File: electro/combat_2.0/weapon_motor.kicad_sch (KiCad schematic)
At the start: 12 parts

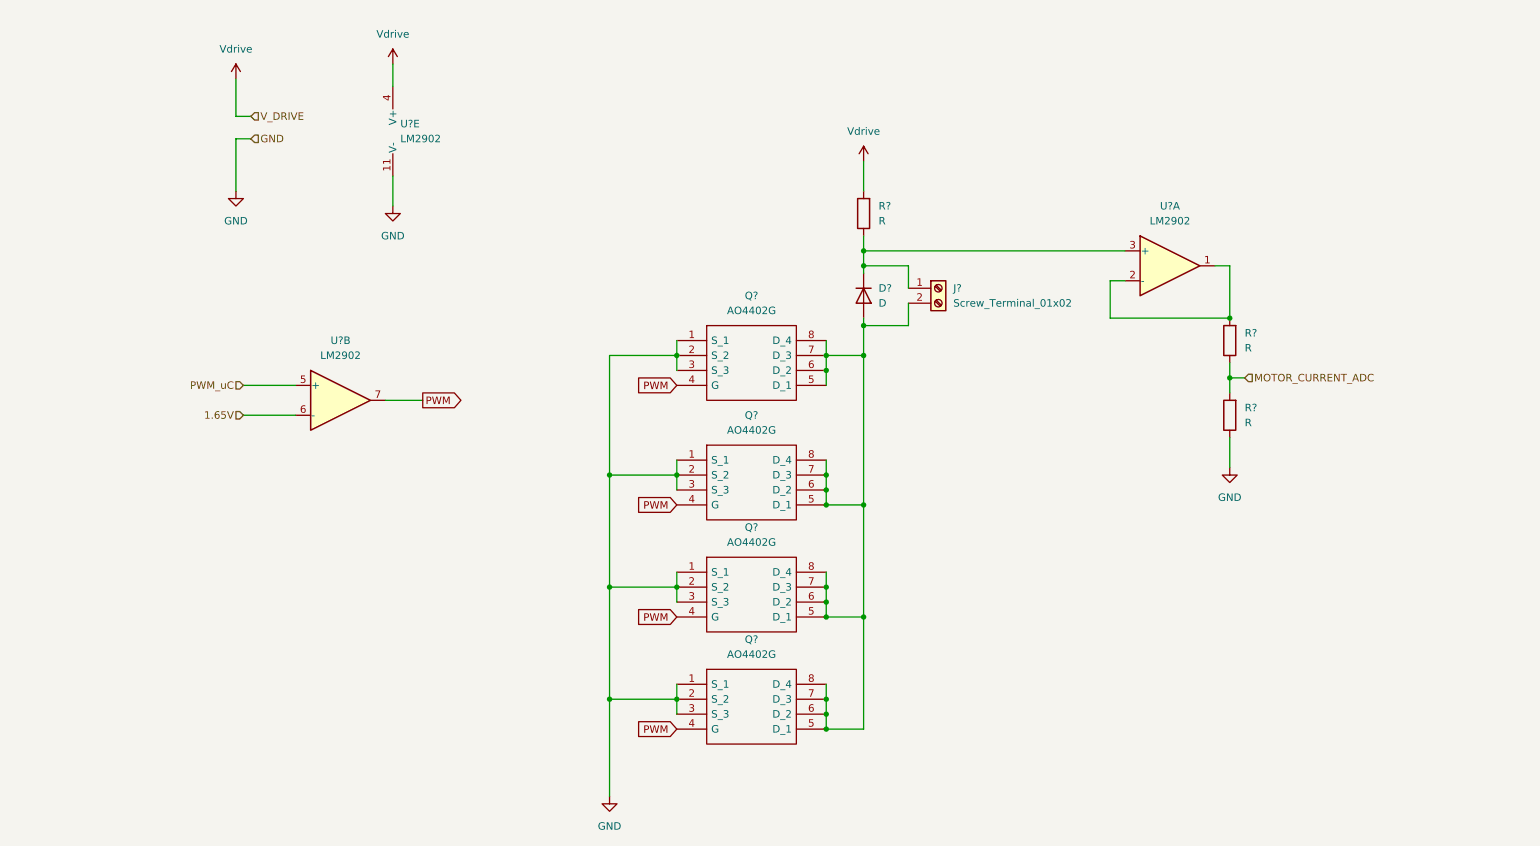
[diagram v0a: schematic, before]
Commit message: 20A Current sensor
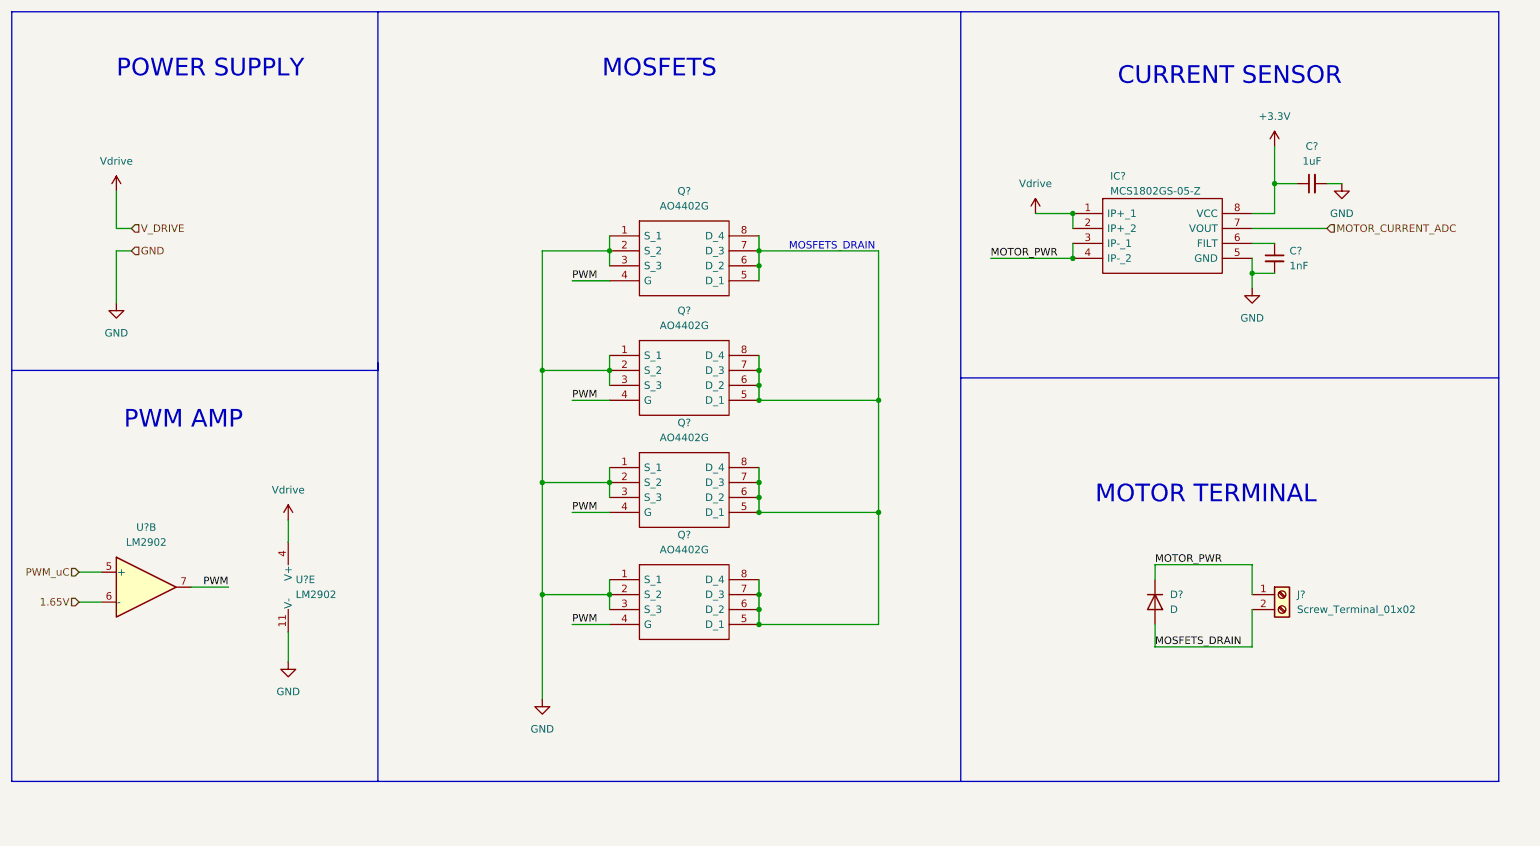
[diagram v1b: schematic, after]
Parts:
- removed R? (x3): R, symbol Device:R
- removed U?: LM2902, symbol Amplifier_Operational:LM2902
- added C?: 1uF, Capacitor_SMD:C_1206_3216Metric, symbol Device:C_Small
- added C?: 1nF, Capacitor_SMD:C_1206_3216Metric, symbol Device:C_Small
- added IC?: MCS1802GS-05-Z, MCS1802GS:SOIC127P600X175-8N, symbol MCS1802GS-05-Z:MCS1802GS-05-Z
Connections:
- net GND: now also C?.2, C?.2, IC?.5 (GND)
- net MOTOR_CURRENT_ADC: now also IC?.7 (VOUT)
- net Vdrive: now also IC?.1 (IP+_1), IC?.2 (IP+_2)
- net MOTOR_PWR: now reaches D?.1 (K), J?.1 (Pin_1)
- net MOTOR_PWR: now also IC?.3 (IP-_1), IC?.4 (IP-_2)
- net at Q?.5 (D_1), Q?.5 (D_1), Q?.5 (D_1)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: no longer D?.2 (A), J?.2 (Pin_2)
- new net: C?.1, IC?.6 (FILT)
- new net +3.3V: C?.1, IC?.8 (VCC)
- new net MOSFETS_DRAIN: D?.2 (A), J?.2 (Pin_2)
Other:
- note added: "CURRENT SENSOR"
- note added: "MOSFETS"
- note added: "MOSFETS_DRAIN"
- note added: "MOTOR TERMINAL"
- note added: "POWER SUPPLY"
- note added: "PWM AMP"
- moved on the sheet: D?, J?, Q?, U?B, U?E

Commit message: PCB V0
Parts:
- added F2: 12A, Capacitor_THT:C_Rect_L13.0mm_W3.0mm_P10.00mm_FKS3_FKP3_MKS4, symbol Device:Polyfuse_Small
- added R3: R, Resistor_SMD:R_0805_2012Metric, symbol Device:R
- C10, C9: renamed from C?; footprint Capacitor_SMD:C_1206_3216Metric -> Capacitor_SMD:C_0805_2012Metric
- D1: renamed from D?; footprint (none) -> Diode_SMD:D_SOD-123F
- J4: renamed from J?; footprint (none) -> TerminalBlock:TerminalBlock_Altech_AK300-2_P5.00mm
- Q1, Q2, Q3, Q4: renamed from Q?; footprint SOIC127P600X175-8N -> MCS1802GS:SOIC127P600X175-8N
- gave numbers to parts that had none: 2
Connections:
- net MOSFETS_DRAIN: now also J4.1 (Pin_1), Q1.5 (D_1), Q1.6 (D_2), Q1.7 (D_3), Q1.8 (D_4), Q2.5 (D_1), Q2.6 (D_2), Q2.7 (D_3), Q2.8 (D_4), Q3.5 (D_1), Q3.6 (D_2), Q3.7 (D_3), Q3.8 (D_4), Q4.5 (D_1), Q4.6 (D_2), Q4.7 (D_3), Q4.8 (D_4); no longer J4.2 (Pin_2)
- net MOTOR_PWR: now also J4.2 (Pin_2), F2.1; no longer IC1.3 (IP-_1), IC1.4 (IP-_2), J4.1 (Pin_1)
- net PWM: now also R3.2; no longer U4.7
- net PWM_uC: now also U4.7, R3.1
- new net: F2.2, IC1.3 (IP-_1), IC1.4 (IP-_2)
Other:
- note added: "Is just 3V3 enough?"
- note removed: "MOSFETS_DRAIN"
- moved on the sheet: J4, U4E

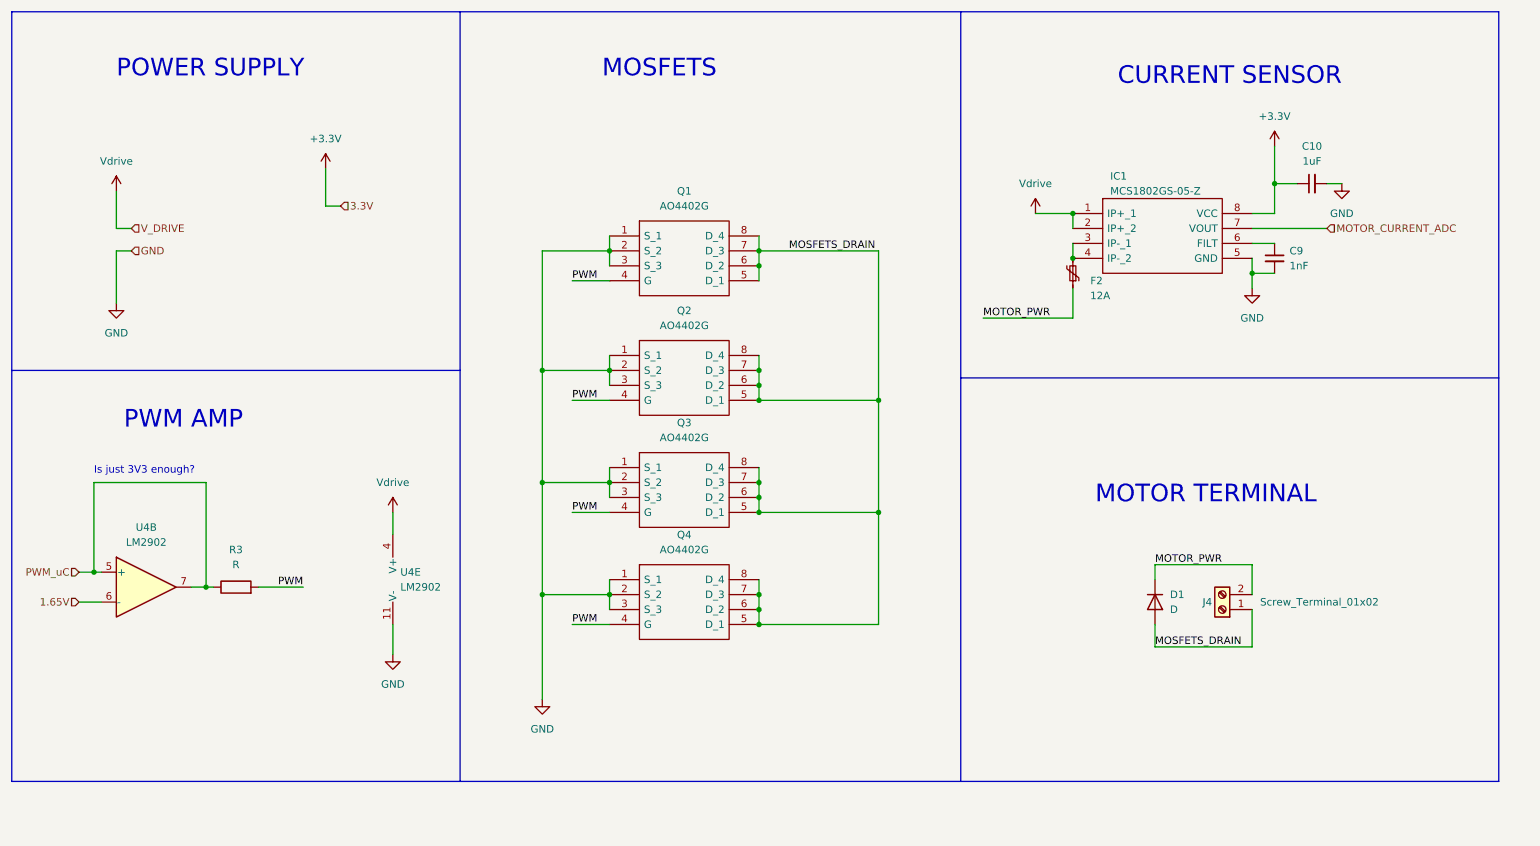
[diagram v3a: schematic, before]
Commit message: Standarized schematic labels
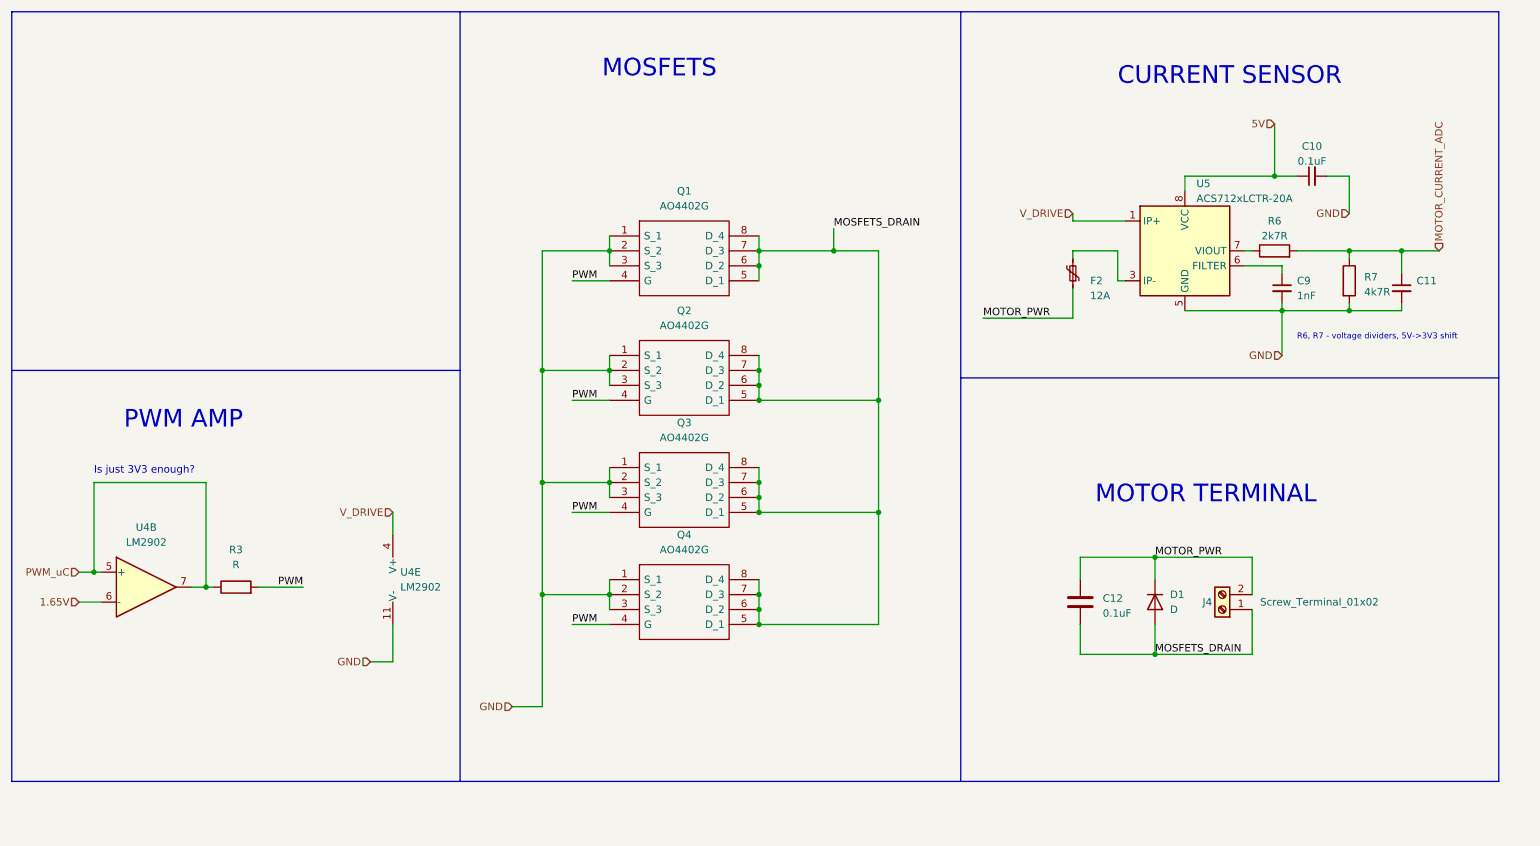
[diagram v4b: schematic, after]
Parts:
- removed IC1: MCS1802GS-05-Z, MCS1802GS:SOIC127P600X175-8N, symbol MCS1802GS-05-Z:MCS1802GS-05-Z
- added C11: ~, Capacitor_SMD:C_0805_2012Metric, symbol Device:C_Small
- added C12: 0.1uF, symbol Device:C
- added R6: 2k7R, symbol Device:R
- added R7: 4k7R, symbol Device:R
- added U5: ACS712xLCTR-20A, Package_SO:SOIC-8_3.9x4.9mm_P1.27mm, symbol Sensor_Current:ACS712xLCTR-20A
- C10: value 1uF -> 0.1uF
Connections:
- net GND: now also C11.2, R7.2, U5.5 (GND)
- net MOSFETS_DRAIN: now also C12.2
- net MOTOR_CURRENT_ADC: now also C11.1, R6.2, R7.1
- net MOTOR_PWR: now also C12.1
- net at F2.2: now also U5.3 (IP-), U5.4 (IP-)
- net at C9.1: now also U5.6 (FILTER)
- net +3.3V renamed 5V
- net 5V: now also U5.8 (VCC)
- net Vdrive renamed V_DRIVE
- net V_DRIVE: now also U5.1 (IP+), U5.2 (IP+)
- new net: R6.1, U5.7 (VIOUT)
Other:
- note added: "R6, R7 - voltage dividers, 5V->3V3 shift"
- note removed: "POWER SUPPLY"
- moved on the sheet: C10, C9

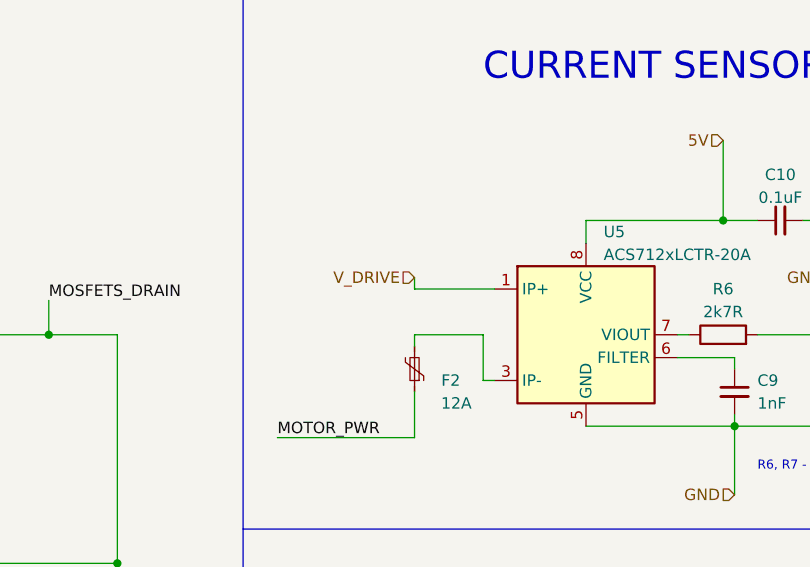
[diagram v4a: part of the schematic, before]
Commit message: Changed resistors to SMD1206 type, hand-soldered version (slightly bigger pads)
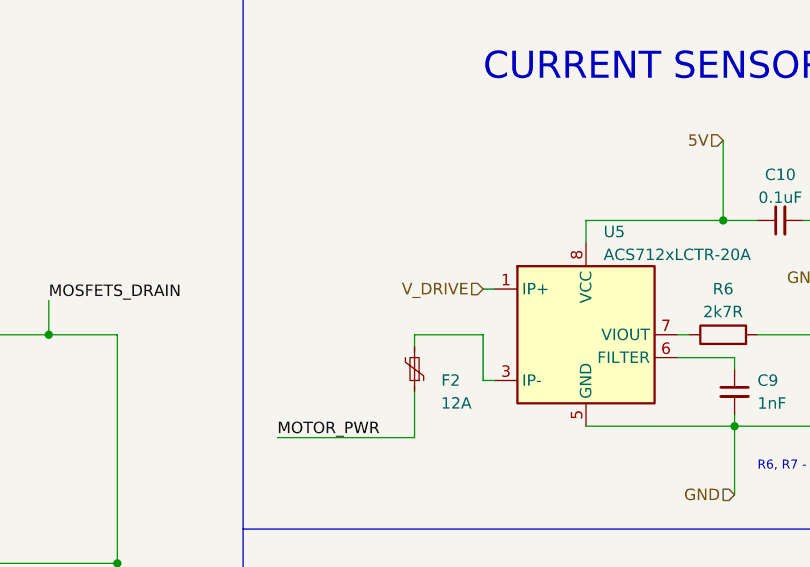
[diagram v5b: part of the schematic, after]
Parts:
- R3: footprint Resistor_SMD:R_0805_2012Metric -> Resistor_SMD:R_1206_3216Metric_Pad1.30x1.75mm_HandSolder
- R6, R7: footprint (none) -> Resistor_SMD:R_1206_3216Metric_Pad1.30x1.75mm_HandSolder
- U4: footprint (none) -> Package_SO:SOIC-14_3.9x8.7mm_P1.27mm
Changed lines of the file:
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@@
     (stroke (width 0) (type default))
   )
-  (wire (pts (xy 205.74 58.42) (xy 214.63 58.42))
+  (wire (pts (xy 213.36 58.42) (xy 214.63 58.42))
     (stroke (width 0) (type default))
   )
@@
   )
   (wire (pts (xy 252.73 73.66) (xy 261.62 73.66))
-    (stroke (width 0) (type default))
-  )
-  (wire (pts (xy 205.74 58.42) (xy 205.74 57.15))
     (stroke (width 0) (type default))
   )
@@
     (effects (font (size 1.27 1.27)) (justify right))
   )
-  (hierarchical_label "V_DRIVE" (shape input) (at 205.74 57.15 180) (fields_autoplaced)
+  (hierarchical_label "V_DRIVE" (shape input) (at 213.36 58.42 180) (fields_autoplaced)
     (effects (font (size 1.27 1.27)) (justify right))
   )
@@
       (effects (font (size 1.27 1.27)))
     )
-    (property "Footprint" "" (at 240.03 65.278 90)
+    (property "Footprint" "Resistor_SMD:R_1206_3216Metric_Pad1.30x1.75mm_HandSolder" (at 240.03 65.278 90)
       (effects (font (size 1.27 1.27)) hide)
     )
@@
       (effects (font (size 1.27 1.27)))
     )
-    (property "Footprint" "Resistor_SMD:R_0805_2012Metric" (at 63.5 122.428 90)
+    (property "Footprint" "Resistor_SMD:R_1206_3216Metric_Pad1.30x1.75mm_HandSolder" (at 63.5 122.428 90)
       (effects (font (size 1.27 1.27)) hide)
     )
@@
       (effects (font (size 1.27 1.27)))
     )
-    (property "Footprint" "" (at 46.99 118.11 0)
+    (property "Footprint" "Package_SO:SOIC-14_3.9x8.7mm_P1.27mm" (at 46.99 118.11 0)
       (effects (font (size 1.27 1.27)) hide)
     )
@@
       (effects (font (size 1.27 1.27)) (justify left))
     )
-    (property "Footprint" "" (at 250.952 68.58 90)
+    (property "Footprint" "Resistor_SMD:R_1206_3216Metric_Pad1.30x1.75mm_HandSolder" (at 250.952 68.58 90)
       (effects (font (size 1.27 1.27)) hide)
     )
@@
       (effects (font (size 1.27 1.27)) (justify left))
     )
-    (property "Footprint" "" (at 91.44 116.84 0)
-      (effects (font (size 1.27 1.27)) hide)
-    )
+    (property "Footprint" "Package_SO:SOIC-14_3.9x8.7mm_P1.27mm" (at 91.44 116.84 0)
+      (effects (font (size 1.27 1.27)) hide)
+    )
